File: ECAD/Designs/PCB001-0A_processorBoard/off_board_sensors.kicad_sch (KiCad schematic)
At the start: 4 parts

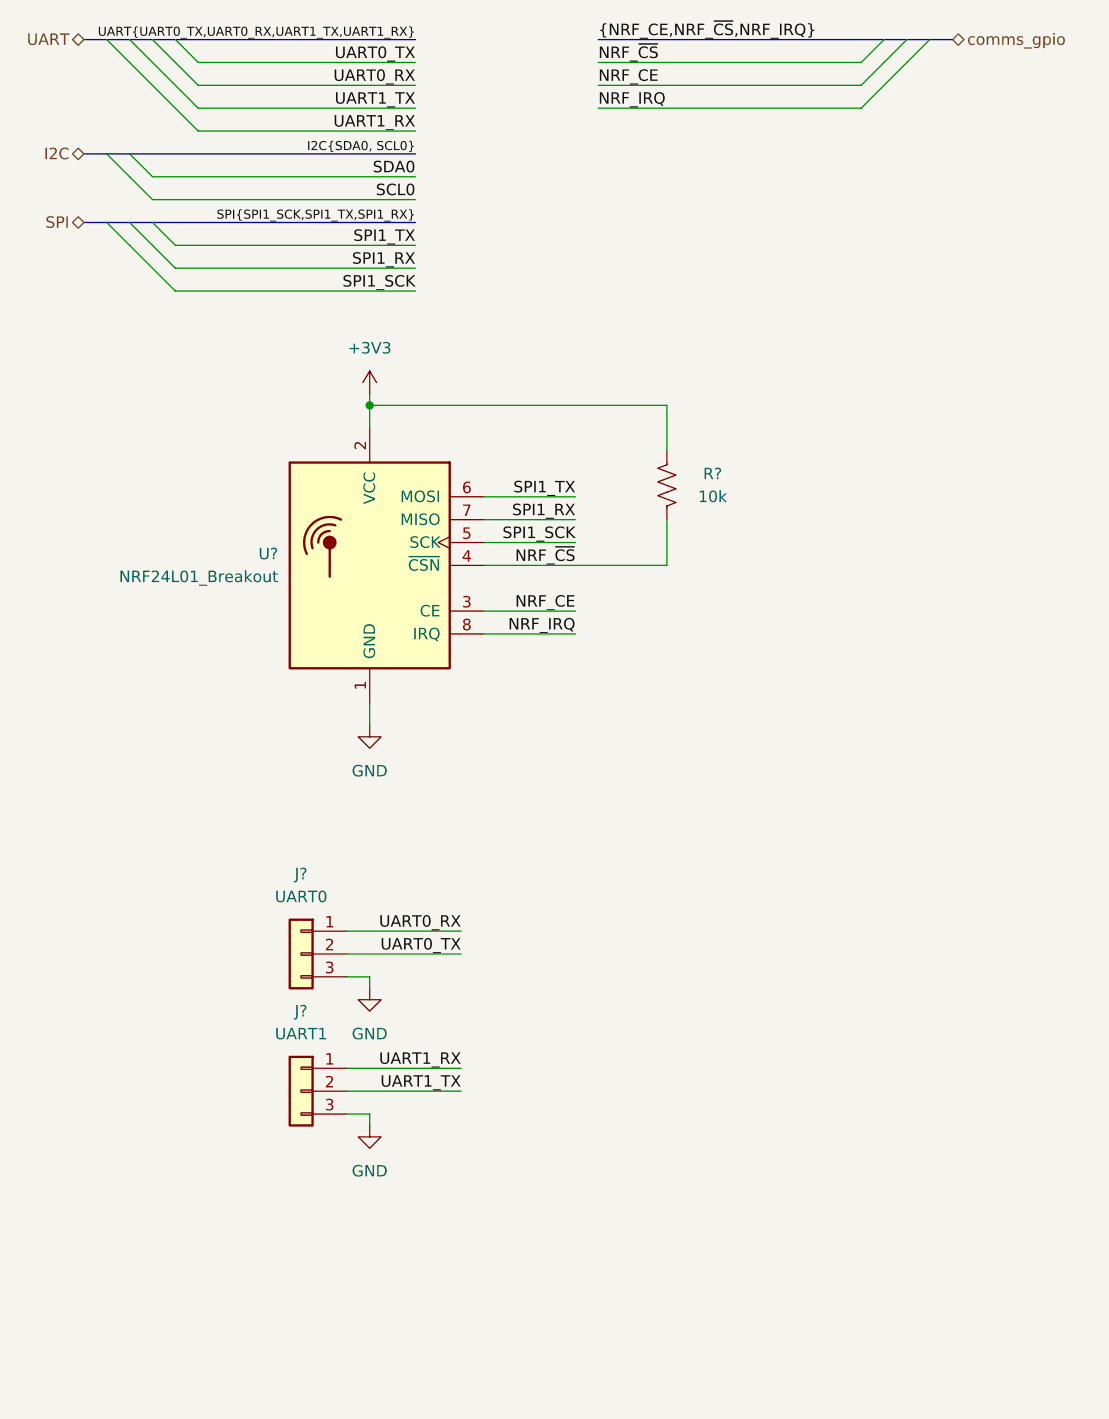
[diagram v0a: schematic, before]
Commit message: added off board sensors page, included more gpio (see google drive), and tracked the gpio better
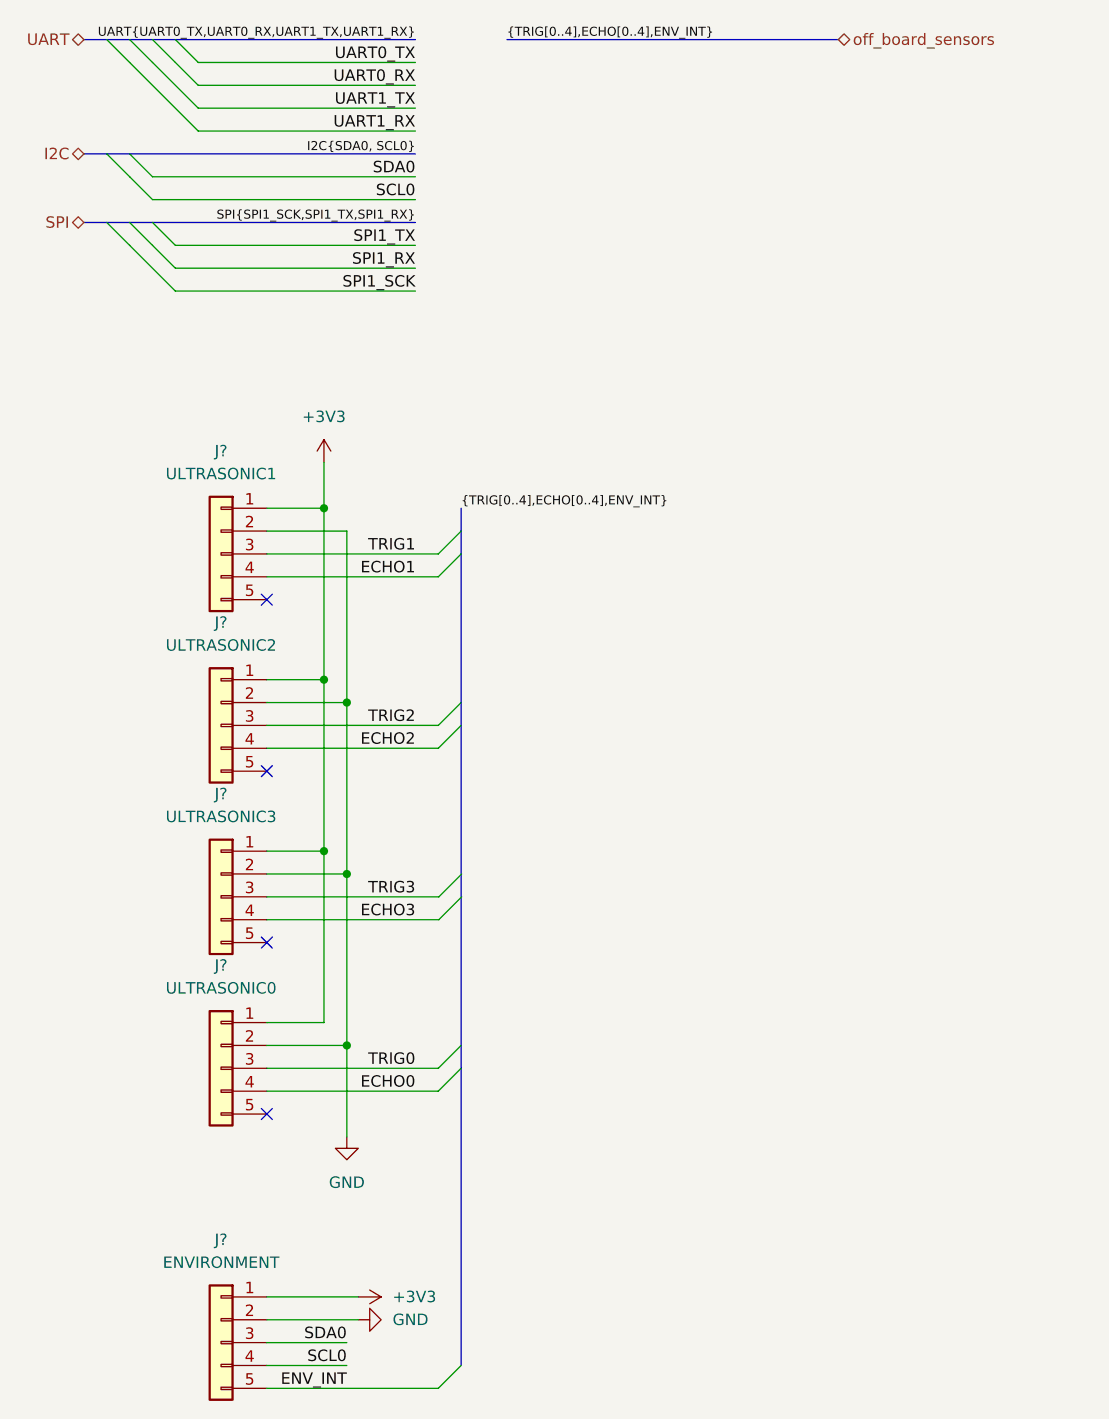
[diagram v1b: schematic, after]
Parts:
- removed J?: UART1, Connector_Molex:Molex_PicoBlade_53047-0310_1x03_P1.25mm_Vertical, symbol Connector_Generic:Conn_01x03
- removed J?: UART0, Connector_Molex:Molex_PicoBlade_53047-0310_1x03_P1.25mm_Vertical, symbol Connector_Generic:Conn_01x03
- removed R?: 10k, Resistor_SMD:R_0402_1005Metric_Pad0.72x0.64mm_HandSolder, symbol Device:R_US
- removed U?: NRF24L01_Breakout, RF_Module:nRF24L01_Breakout, symbol RF:NRF24L01_Breakout
- added J?: ULTRASONIC0, Connector_Molex:Molex_PicoBlade_53047-0510_1x05_P1.25mm_Vertical, symbol Connector_Generic:Conn_01x05
- added J?: ULTRASONIC3, Connector_Molex:Molex_PicoBlade_53047-0510_1x05_P1.25mm_Vertical, symbol Connector_Generic:Conn_01x05
- added J?: ULTRASONIC2, Connector_Molex:Molex_PicoBlade_53047-0510_1x05_P1.25mm_Vertical, symbol Connector_Generic:Conn_01x05
- added J?: ENVIRONMENT, Connector_Molex:Molex_PicoBlade_53047-0510_1x05_P1.25mm_Vertical, symbol Connector_Generic:Conn_01x05
- added J?: ULTRASONIC1, Connector_Molex:Molex_PicoBlade_53047-0510_1x05_P1.25mm_Vertical, symbol Connector_Generic:Conn_01x05
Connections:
- net +3V3: now also J?.1 (Pin_1), J?.1 (Pin_1), J?.1 (Pin_1), J?.1 (Pin_1), J?.1 (Pin_1)
- net GND: now also J?.2 (Pin_2), J?.2 (Pin_2), J?.2 (Pin_2), J?.2 (Pin_2), J?.2 (Pin_2)
- net SCL0: now also J?.4 (Pin_4)
- net SDA0: now also J?.3 (Pin_3)
- new net ECHO0: J?.4 (Pin_4)
- new net ECHO1: J?.4 (Pin_4)
- new net ECHO2: J?.4 (Pin_4)
- new net ECHO3: J?.4 (Pin_4)
- new net ENV_INT: J?.5 (Pin_5)
- new net TRIG0: J?.3 (Pin_3)
- new net TRIG1: J?.3 (Pin_3)
- new net TRIG2: J?.3 (Pin_3)
- new net TRIG3: J?.3 (Pin_3)
- no-connect marks 0 -> 4
